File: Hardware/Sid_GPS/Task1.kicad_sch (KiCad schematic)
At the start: 26 parts, among them J3 Conn_01x04, J4 Conn_01x04, SW1 SW_SPDT, U1 STM32F103C8Tx, U3 ZED-F9P, Y1 16Mhz

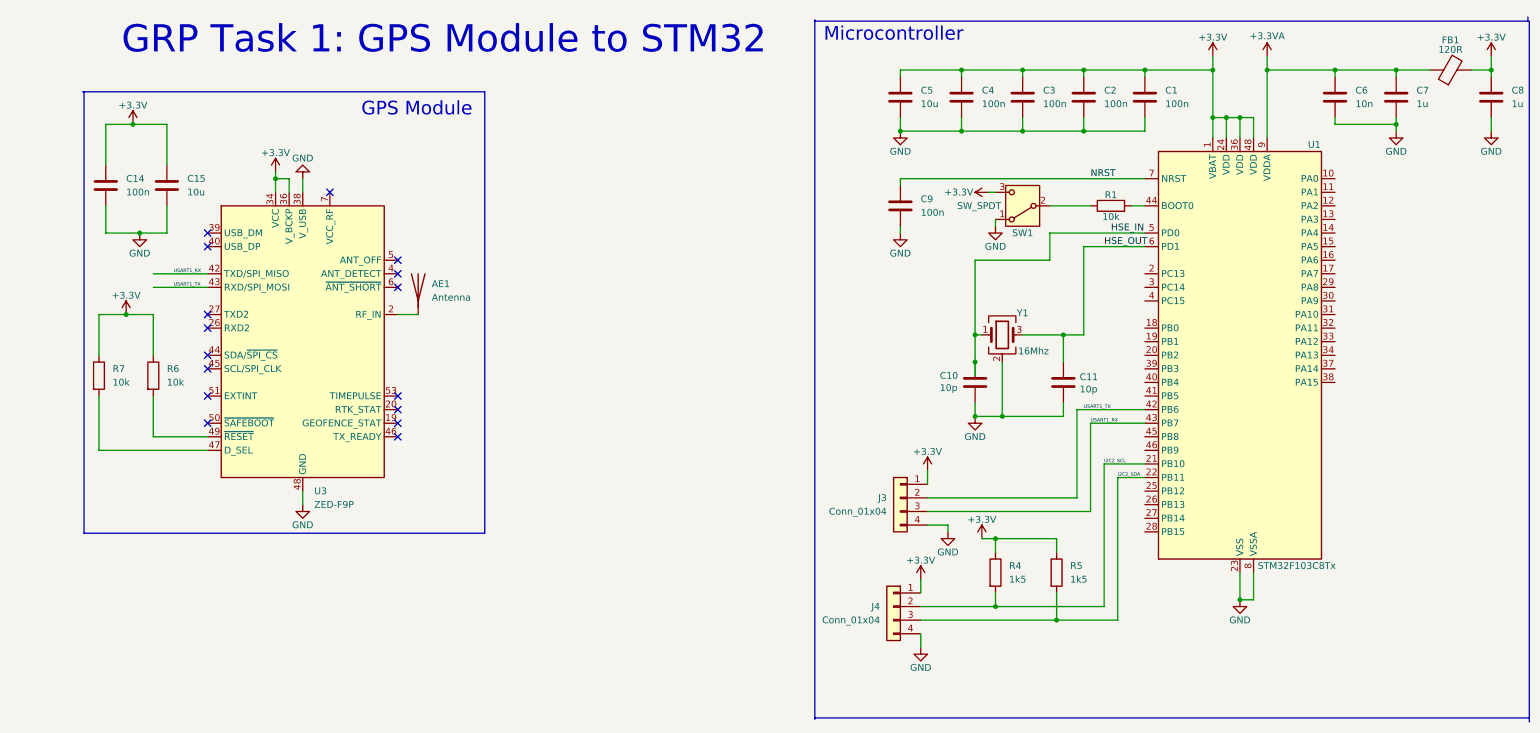
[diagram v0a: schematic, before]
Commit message: Cleaned up GPS and STM32
Made my schematic more legible before incorporating antenna shielding
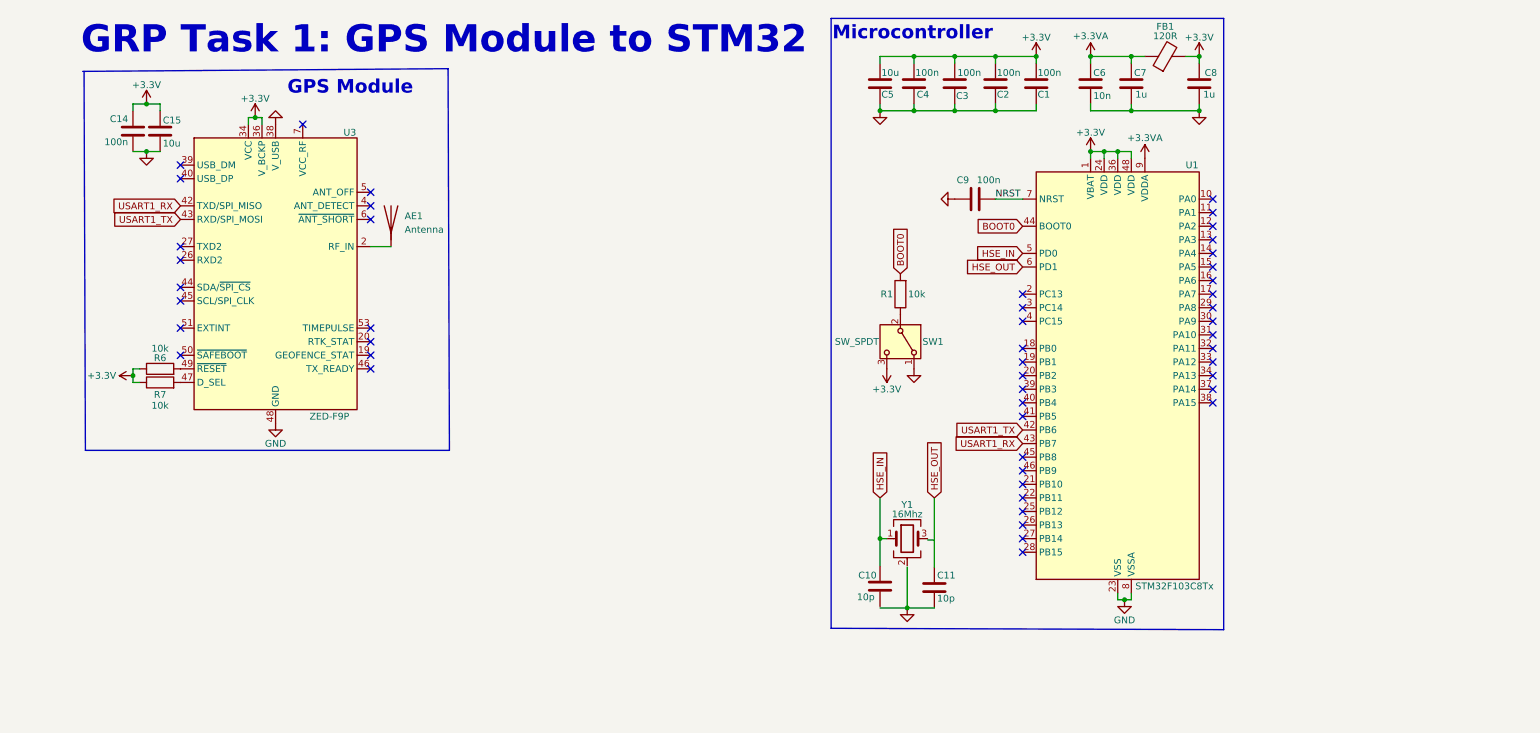
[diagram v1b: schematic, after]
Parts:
- removed J3, J4: Conn_01x04, symbol Connector_Generic:Conn_01x04
- removed R4, R5: 1k5, symbol Device:R
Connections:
- net GND: now also C9.1; no longer C10.2, C9.2, Y1.2 (G), Y1.4 (G)
- net HSE_OUT: no longer C11.1, Y1.3
- net NRST: now also C9.2; no longer C9.1
- net BOOT0: now reaches R1.2, U1.44 (BOOT0)
- net I2C2_SCL: no longer names the net of U1.21 (PB10)
- net I2C2_SDA: no longer names the net of U1.22 (PB11)
- new net: Y1.2 (G), Y1.4 (G)
- no-connect marks 16 -> 49
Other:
- moved on the sheet: AE1, C1, C10, C11, C14, C15, C2, C3, C4, C5, C6, C7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
